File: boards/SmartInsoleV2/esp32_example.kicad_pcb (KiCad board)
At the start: 2 copper layers, 57.2 x 79.5 mm, 104 parts, among them J1 Screw_Terminal_01x02, J2 USB_B_Micro, J3 Conn_01x05_Female, J4 Screw_Terminal_01x02, J5 Conn_01x09_Female, J6 Conn_01x08_Female, J7 Conn_ARM_JTAG_SWD_10, J8 Screw_Terminal_01x02, Q1 AO4485, Q2 SS8050-G, Q3 SS8050-G, SW1 SW_Push, SW2 SW_Push, U1 INA240A1D, U2 MAX14871EUE+, U3 OPA2340, U4 INA240A1D, U5 MAX14871EUE+, U6 TPS62933ODRLR, U7 ESP32-S3-WROOM-1-N16R2

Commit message: a little progress
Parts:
- removed C10, C11, C12: 10u, Resistor_SMD:R_1206_3216Metric
- removed C13, C14, C15, C21, C25, C5, C6, C9: 100n, Capacitor_SMD:C_0805_2012Metric
- removed C16, C20: 10u, Capacitor_SMD:C_0805_2012Metric
- removed C17, C22, C7, C8: DNP, Capacitor_SMD:C_0805_2012Metric
- removed C26, C27: 33u, Capacitor_SMD:C_0805_2012Metric
- removed D2: D_Zener, local_footprints:SOD-123_ONS
- removed D4: D_Schottky, Diode_SMD:D_SMA
- removed F1: Fuse, Fuse:Fuseholder_Littelfuse_Nano2_154x
- removed J5: Conn_01x09_Female, Connector_PinHeader_2.54mm:PinHeader_1x09_P2.54mm_Vertical
- removed J6: Conn_01x08_Female, Connector_PinHeader_2.54mm:PinHeader_1x08_P2.54mm_Vertical
- removed J8: Screw_Terminal_01x02, TerminalBlock_Phoenix:TerminalBlock_Phoenix_MKDS-1,5-2-5.08_1x02_P5.08mm_Horizontal
- removed JP3: SolderJumper_2_Open, Jumper:SolderJumper-2_P1.3mm_Open_TrianglePad1.0x1.5mm
- removed L1: 4.7u, Inductor_SMD:L_Taiyo-Yuden_NR-60xx
- removed Q1: AO4485, local_footprints:SO8SOP-8L_AOS
- removed R23, R26: DNP, Resistor_SMD:R_0805_2012Metric
- removed R27, R28, R29: 100k, Resistor_SMD:R_0805_2012Metric
- removed R30: 31.3k, Resistor_SMD:R_0805_2012Metric
- removed R31: 10.0k, Resistor_SMD:R_0805_2012Metric
- removed R9: 10k, Resistor_SMD:R_0805_2012Metric
- removed TP1, TP10, TP12, TP13, TP2, TP3, TP4, TP5, TP6, TP7, TP8, TP9: TestPoint, TestPoint:TestPoint_Keystone_5010-5014_Multipurpose
- removed TP11: TestPoint, TestPoint:TestPoint_Pad_D2.0mm
- removed U2, U5: MAX14871EUE+, local_footprints:21-0108_U16E&plus_3_MXM
- removed U4: INA240A1D, Package_SO:SOIC-8_3.9x4.9mm_P1.27mm
- removed U6: TPS62933ODRLR, local_footprints:SOT5X3-8_DRL_TEX
- added SW3: SW_Push, Button_Switch_SMD:SW_SPST_B3S-1000, F.Cu at (97.4, 85.1)
- added SW4: SW_Push, Button_Switch_SMD:SW_SPST_B3S-1000, F.Cu at (97.4, 93.6)
- C1, C2: value 10u -> 1uF; footprint Resistor_SMD:R_1206_3216Metric -> Capacitor_SMD:C_0603_1608Metric
- C3: value 10u -> 10uF; footprint Resistor_SMD:R_1206_3216Metric -> Capacitor_SMD:C_0603_1608Metric
- C4: value 100n -> 10uF; footprint Capacitor_SMD:C_0805_2012Metric -> Capacitor_SMD:C_0603_1608Metric
- D3: value BAT54S -> LED; footprint Package_TO_SOT_SMD:SOT-23 -> LED_SMD:LED_0603_1608Metric
- J1: value Screw_Terminal_01x02 -> Conn_01x02_Pin; footprint TerminalBlock_Phoenix:TerminalBlock_Phoenix_MKDS-1,5-2-5.08_1x02_P5.08mm_Horizontal -> Connector_JST:JST_PH_B2B-PH-K_1x02_P2.00mm_Vertical
- J4: value Screw_Terminal_01x02 -> Conn_02x10_Odd_Even; footprint TerminalBlock_Phoenix:TerminalBlock_Phoenix_MKDS-1,5-2-5.08_1x02_P5.08mm_Horizontal -> Connector_PinHeader_2.54mm:PinHeader_2x10_P2.54mm_Vertical
- JP1, R12: moved to F.Cu
- R1, R15: value 20m -> 1k; footprint Resistor_SMD:R_1206_3216Metric -> Resistor_SMD:R_0603_1608Metric
- R10, R11: value 100k -> 1k; footprint Resistor_SMD:R_0805_2012Metric -> Resistor_SMD:R_0603_1608Metric
- R16, R2: value DNP -> 1k; footprint Resistor_SMD:R_0805_2012Metric -> Resistor_SMD:R_0603_1608Metric
- R20: value 1k -> 1M; footprint Resistor_SMD:R_0805_2012Metric -> Resistor_SMD:R_0603_1608Metric
- R21: value 0 -> 200k; footprint Resistor_SMD:R_0805_2012Metric -> Resistor_SMD:R_0603_1608Metric
- R22: value DNP -> 5.1k; footprint Resistor_SMD:R_0805_2012Metric -> Resistor_SMD:R_0603_1608Metric
- R3, R4: value 4.7k -> 1k; footprint Resistor_SMD:R_0805_2012Metric -> Resistor_SMD:R_0603_1608Metric
- R5: footprint Resistor_SMD:R_0805_2012Metric -> Resistor_SMD:R_0603_1608Metric
- R6, R8: value 100k -> 5k; footprint Resistor_SMD:R_0805_2012Metric -> Resistor_SMD:R_0603_1608Metric
- R7: value 0 -> 1k; footprint Resistor_SMD:R_0805_2012Metric -> Resistor_SMD:R_0603_1608Metric
- U1: value INA240A1D -> MPU-6050; footprint Package_SO:SOIC-8_3.9x4.9mm_P1.27mm -> Sensor_Motion:InvenSense_QFN-24_4x4mm_P0.5mm
- U3: value OPA2340 -> TLV75801PDRV; footprint Package_SO:SOIC-8_3.9x4.9mm_P1.27mm -> Package_SON:WSON-6-1EP_2x2mm_P0.65mm_EP1x1.6mm
- moved H2 120.1 mm to (218.9, 52.4)
- moved H4 108.5 mm to (221.2, 119.6)
- moved J2 103.3 mm to (207.3, 69.5), turned to 90 degrees
- moved R11 83.7 mm to (185.2, 87.7), turned to -90 degrees
- moved J4 75.9 mm to (167.8, 96.4), turned to 90 degrees
- moved R1 74.6 mm to (167.7, 87.7), turned to -90 degrees
- moved R15 74.2 mm to (187.6, 87.7), turned to -90 degrees
- moved JP1 72.4 mm to (99.0, 104.2), turned to 0 degrees
- moved R20 68.3 mm to (132.9, 97.9), turned to 0 degrees
- moved R2 68.3 mm to (170.2, 87.7), turned to -90 degrees
- moved R16 67.6 mm to (190.0, 87.7), turned to -90 degrees
- moved SW2 67.3 mm to (97.4, 76.7), turned to 0 degrees
- moved Q3 63.6 mm to (94.3, 104.8), turned to 0 degrees
- moved Q2 63.6 mm to (94.3, 100.2), turned to 0 degrees
- moved R21 61.8 mm to (132.9, 100.4), turned to 0 degrees
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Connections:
- C1 pad 1: +BATT -> /End Hike
- C2 pad 1: +BATT -> /Start Hike
- C3 pad 1: +BATT -> /POWER FROM BATTERY
- C4 pad 1: +BATT -> +3V3
- D3 pad 2: +3V3 -> Net-(D3-A)
- J1 pad 1: GND -> /POWER FROM BATTERY
- J1 pad 2: Net-(F1-Pad1) -> GND
- J4 pad 1: /M1- -> /PRESS1
- J4 pad 2: Net-(J4-Pad2) -> GND
- R1 pad 1: Net-(J4-Pad2) -> /PRESS1
- R1 pad 2: /M1+ -> +3V3
- R10 pad 1: /M1_FAULT -> /PRESS7
- R11 pad 1: Net-(R11-Pad1) -> /PRESS8
- R15 pad 1: Net-(J8-Pad2) -> /PRESS9
- R15 pad 2: /M2+ -> +3V3
- R16 pad 1: GND -> /PRESS10
- R16 pad 2: Net-(R16-Pad2) -> +3V3
- R2 pad 1: GND -> /PRESS2
- R2 pad 2: Net-(R2-Pad2) -> +3V3
- R20 pad 1: Net-(R20-Pad1) -> Net-(U3-FB)
- R20 pad 2: Net-(C15-Pad1) -> +3V3
- R21 pad 1: Net-(C15-Pad1) -> GND
- R21 pad 2: Net-(C17-Pad1) -> Net-(U3-FB)
- R22 pad 1: +BATT -> +3V3
- R22 pad 2: Net-(R22-Pad2) -> Net-(D3-A)
- R3 pad 1: +3V3 -> /PRESS3
- R3 pad 2: /CAMERA_SDA -> +3V3
- R4 pad 1: +3V3 -> /PRESS4
- R4 pad 2: /CAMERA_SCL -> +3V3
- R5 pad 1: Net-(R5-Pad1) -> /PRESS5
- R5 pad 2: Net-(C6-Pad1) -> +3V3
- R6 pad 2: GND -> /End Hike
- R7 pad 1: Net-(C6-Pad1) -> /PRESS6
- R7 pad 2: Net-(C7-Pad1) -> +3V3
- R8 pad 1: +BATT -> Net-(R8-Pad1)
- R8 pad 2: /VBAT_SENSE -> /Start Hike
- U1 pad 1: Net-(J4-Pad2) -> unconnected-(U1-CLKIN-Pad1)
- U1 pad 2: GND -> unconnected-(U1-NC-Pad2)
- U1 pad 3: GND -> unconnected-(U1-NC-Pad3)
- U1 pad 4: GND -> unconnected-(U1-NC-Pad4)
- U1 pad 5: Net-(R5-Pad1) -> unconnected-(U1-NC-Pad5)
- U1 pad 6: +3V3 -> unconnected-(U1-AUX_DA-Pad6)
- U1 pad 7: +3V3 -> unconnected-(U1-AUX_CL-Pad7)
- U1 pad 8: /M1+ -> +3V3
- U3 pad 1: /I_M_1 -> +3V3
- U3 pad 2: /I_M_1 -> Net-(U3-FB)
- U3 pad 3: Net-(C7-Pad1) -> GND
- U3 pad 4: GND -> /POWER FROM BATTERY
- U3 pad 5: Net-(C17-Pad1) -> unconnected-(U3-DNC-Pad5)
- U3 pad 6: /I_M_2 -> /POWER FROM BATTERY
- U3 pad 7: /I_M_2 -> GND
- U7 pad 10: /GPIO17 -> /End Hike
- U7 pad 11: /GPIO18 -> /PRESS1
- U7 pad 12: /M1_FAULT -> /PRESS2
- U7 pad 17: /M1_EN -> /PRESS3
- U7 pad 18: /M1_PWM -> /PRESS4
- U7 pad 19: /M1_DIR -> /PRESS5
- U7 pad 20: /M2_FAULT -> /PRESS6
- U7 pad 21: /M2_EN -> /PRESS7
- U7 pad 22: /M2_PWM -> /PRESS8
- U7 pad 23: /M2_DIR -> /PRESS9
- U7 pad 24: /CAMERA_CS -> /PRESS10
- U7 pad 25: /CAMERA_MOSI -> unconnected-(U7-IO48-Pad25)
- U7 pad 28: /CAMERA_MISO -> /CS
- U7 pad 29: /CAMERA_SCK -> /MISO
- U7 pad 30: /CAMERA_SDA -> /MOSI
- U7 pad 31: /CAMERA_SCL -> /SCLK
- U7 pad 38: /I_M_1 -> /SCL_6050
- U7 pad 39: /I_M_2 -> /SDA_6050
- U7 pad 5: /GPIO5 -> unconnected-(U7-IO5-Pad5)
- U7 pad 6: /GPIO6 -> unconnected-(U7-IO6-Pad6)
- U7 pad 7: /GPIO7 -> unconnected-(U7-IO7-Pad7)
- U7 pad 8: /GPIO15 -> unconnected-(U7-IO15-Pad8)
- U7 pad 9: /GPIO16 -> /Start Hike
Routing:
- net +3V3: track 283.9 -> 0.00 mm, vias 21 -> 0
- net /M1_FAULT: track 70.8 -> 0.00 mm, vias 2 -> 0
- net /I_M_2: track 67.9 -> 0.00 mm, vias 2 -> 0
- net /M1_EN: track 64.0 -> 0.00 mm
- net /I_M_1: track 62.9 -> 0.00 mm, vias 2 -> 0
- net /M1_PWM: track 60.5 -> 0.00 mm
- net /M1_DIR: track 57.4 -> 0.00 mm
- net Net-(R5-Pad1): track 53.0 -> 0.00 mm
- net /M2_DIR: track 52.4 -> 0.00 mm
- net /M2_PWM: track 51.4 -> 0.00 mm
- net +BATT: track 50.1 -> 0.00 mm, vias 34 -> 0
- net /M2_EN: track 48.9 -> 0.00 mm
- net /M2_FAULT: track 48.3 -> 0.00 mm
- net /CAMERA_CS: track 48.2 -> 0.00 mm
- net /CAMERA_MOSI: track 44.8 -> 0.00 mm
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- removed copper zone on B.Cu, net +3V3
- removed copper zone on F.Cu, net +3V3
- removed copper zone on B.Cu, net +BATT
- removed copper zone on F.Cu, net +BATT
- removed copper zone on F.Cu, net /M1+
- removed copper zone on F.Cu, net /M1-
- removed copper zone on F.Cu, net /M2+
- removed copper zone on F.Cu, net /M2-
- removed copper zone on B.Cu, net GND
- removed copper zone on F.Cu, net GND
- removed copper zone on F.Cu, net Net-(C25-Pad2)
- removed copper zone on F.Cu, net Net-(C26-Pad1)
- removed copper zone on F.Cu, net Net-(F1-Pad1)
- removed copper zone on F.Cu, net Net-(F1-Pad2)
- removed copper zone on F.Cu, net Net-(J4-Pad2)
- removed copper zone on F.Cu, net Net-(J8-Pad2)
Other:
- board outline removed
- board text removed: "+"
- board text removed: "-"
- board text removed: "ESP32 Motor Controller Rev A Jason Paximadas"

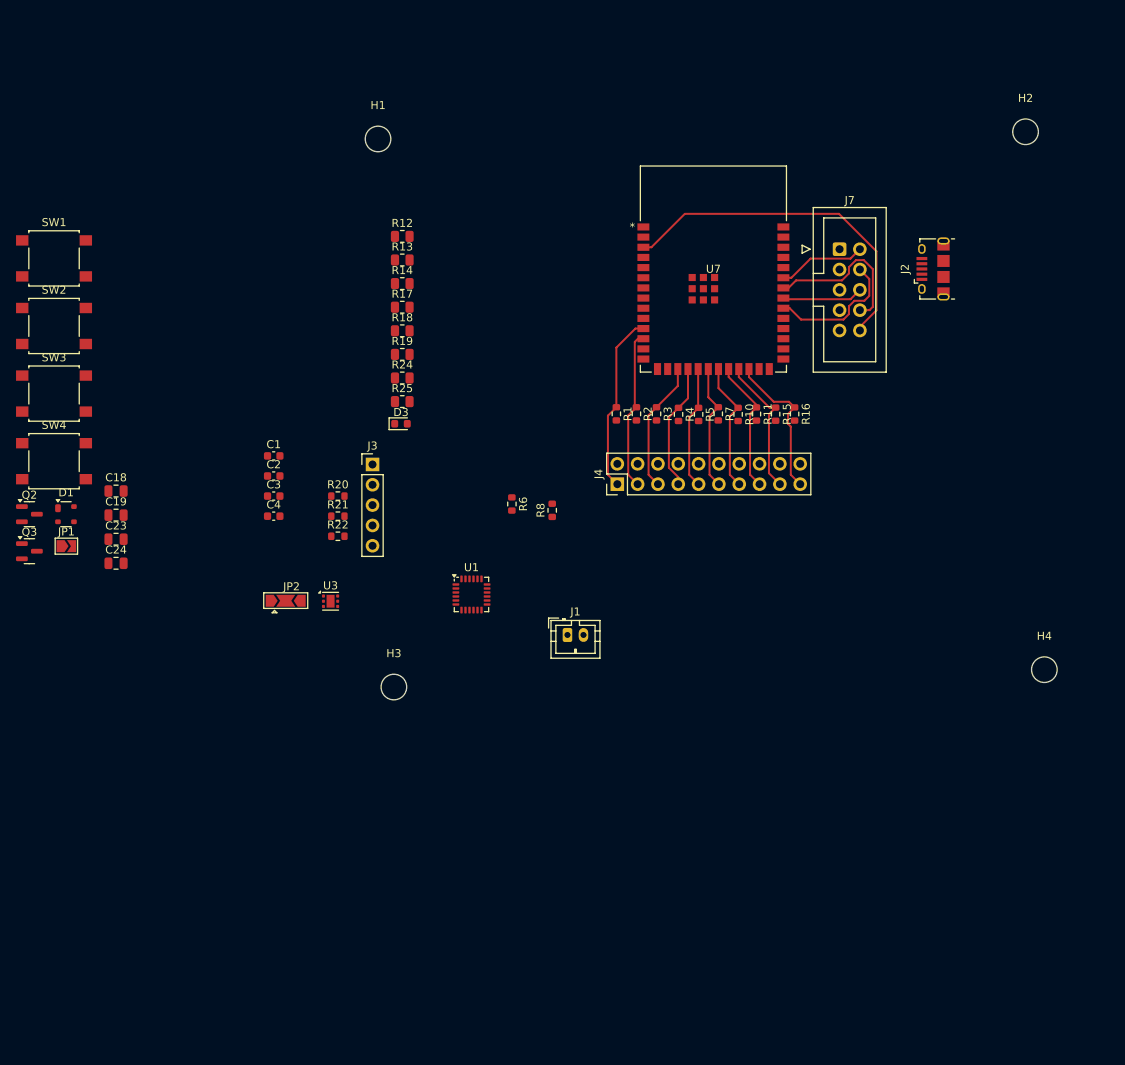
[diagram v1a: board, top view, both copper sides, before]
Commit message: Most of routing done
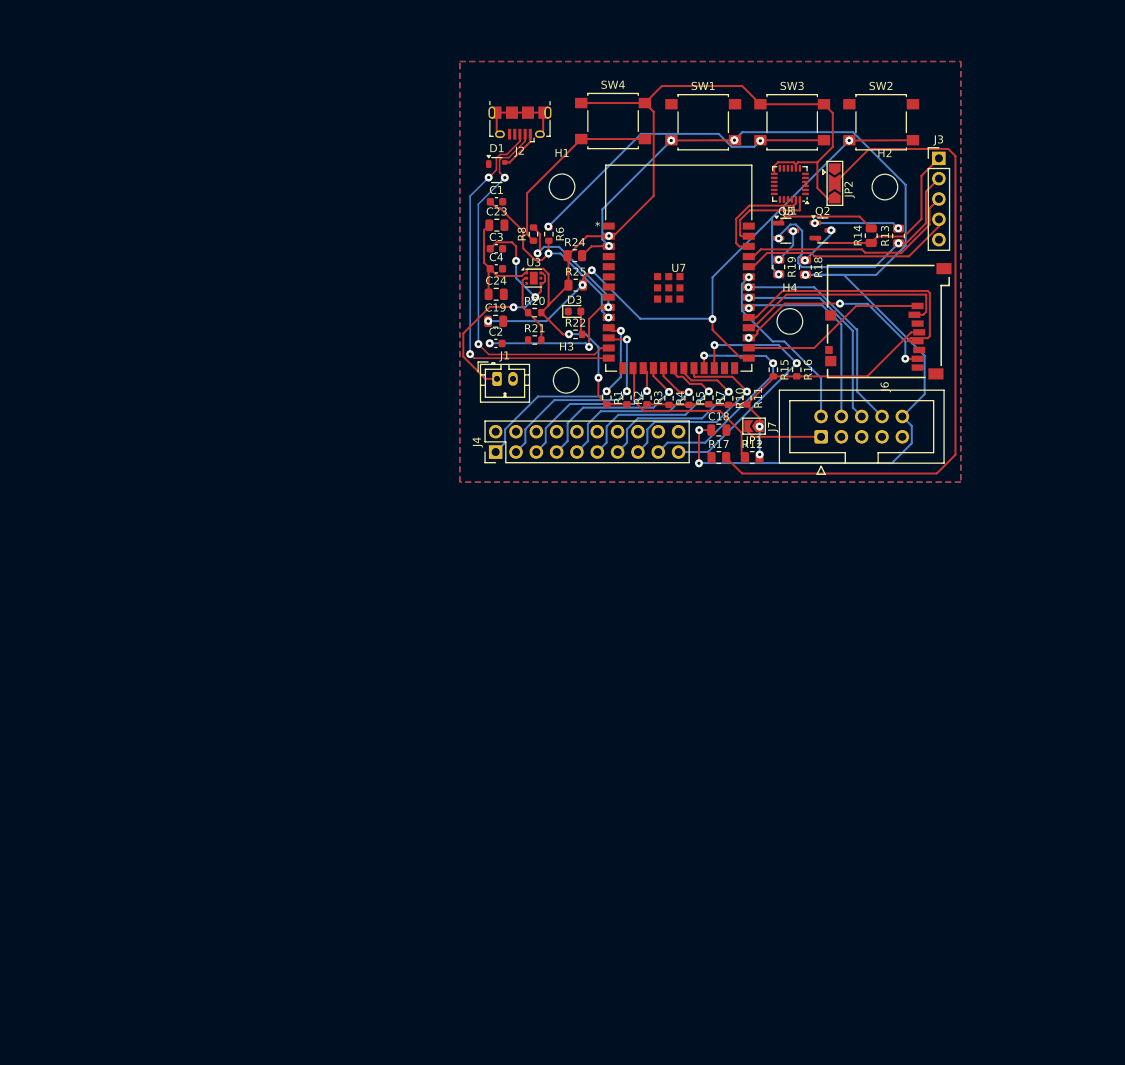
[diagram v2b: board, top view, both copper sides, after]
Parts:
- added J6: PJS008U-3000-0, MEM2051-00-195-00-A:GCT_MEM2051-00-195-00-A, F.Cu at (201.7, 76.1)
- moved SW2 106.5 mm to (200.8, 51.2)
- moved Q2 105.3 mm to (193.5, 64.7)
- moved Q3 102.7 mm to (188.9, 64.8)
- moved SW3 98.3 mm to (189.7, 51.2)
- moved JP1 87.3 mm to (184.9, 89.2), turned to 180 degrees
- moved JP2 86.2 mm to (195.0, 58.8), turned to -90 degrees
- moved SW1 82.9 mm to (178.6, 51.2)
- moved SW4 81.8 mm to (167.3, 51.0)
- moved J3 80.5 mm to (208.0, 55.7)
- moved C18 75.7 mm to (180.5, 89.7)
- moved D1 68.9 mm to (152.8, 57.2)
- moved U1 64.9 mm to (189.4, 58.9), turned to 180 degrees
- moved R13 62.1 mm to (203.0, 65.4), turned to 90 degrees
- moved C23 61.7 mm to (152.8, 64.1)
- moved R14 58.9 mm to (199.6, 65.4), turned to 90 degrees
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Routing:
- net +3V3: track 0.00 -> 174.3 mm, vias 0 -> 5
- net /CHIP_PU: track 43.6 -> 140.3 mm, vias 0 -> 6
- net /GPIO0_STRAPPING: track 0.00 -> 86.1 mm, vias 0 -> 6
- net Net-(JP2-C): track 0.00 -> 85.0 mm
- net /D+: track 0.00 -> 48.1 mm, vias 0 -> 2
- net /D-: track 0.00 -> 47.3 mm, vias 0 -> 2
- net Net-(R6-Pad1): track 0.00 -> 40.2 mm, vias 0 -> 2
- net /Start Hike: track 0.00 -> 36.8 mm, vias 0 -> 4
- net /POWER FROM BATTERY: track 0.00 -> 34.5 mm, vias 0 -> 3
- net /SCLK: track 0.00 -> 33.8 mm
- net /DTR: track 0.00 -> 33.1 mm, vias 0 -> 2
- net /TX: track 0.00 -> 28.3 mm
- net /MOSI: track 0.00 -> 27.7 mm
- net /MISO: track 0.00 -> 27.3 mm, vias 0 -> 3
- net /RX: track 0.00 -> 27.1 mm
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- added copper zone on B.Cu, net GND
- added copper zone on F.Cu, net GND

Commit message: added changes but not finished
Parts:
- removed H1, H2, H3, H4: MountingHole, MountingHole:MountingHole_3.2mm_M3
- removed SW3, SW4: SW_Push, Button_Switch_SMD:SW_SPST_B3S-1000
- added J5: Conn_01x02_Pin, Connector_PinHeader_2.54mm:PinHeader_1x02_P2.54mm_Vertical, F.Cu at (162.8, 60.0)
- added J8: Conn_01x02_Pin, Connector_PinHeader_2.54mm:PinHeader_1x02_P2.54mm_Vertical, F.Cu at (162.4, 56.0)
- moved C23 10.9 mm to (163.2, 67.2)
- moved J2 7.88 mm to (155.5, 59.2)
- moved C1 7.50 mm to (157.5, 66.9)
- moved D1 6.56 mm to (152.7, 63.7)
- moved R24 5.45 mm to (161.8, 73.3)
- moved R6 5.35 mm to (159.3, 70.5)
- moved R8 5.35 mm to (157.4, 70.5)
- moved U3 5.24 mm to (156.1, 75.8)
- moved R25 4.80 mm to (163.2, 76.3)
- moved D3 3.94 mm to (163.2, 78.7)
- moved R20 3.82 mm to (158.8, 78.6)
- moved C19 3.15 mm to (154.5, 78.6)
- moved R22 2.91 mm to (163.2, 80.6)
- moved C2 2.52 mm to (154.6, 80.5)
- moved R21 2.51 mm to (158.9, 80.5)
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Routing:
- net +3V3: track 174.3 -> 58.6 mm, vias 5 -> 10
- net Net-(J8-Pin_1): track 23.8 -> 1.13 mm
- net /POWER FROM BATTERY: track 34.5 -> 24.6 mm, vias 3 -> 2
- net /D+: track 48.1 -> 40.8 mm
- net /End Hike: track 26.0 -> 19.9 mm
- net /D-: track 47.3 -> 41.2 mm
- net Net-(J5-Pin_1): track 40.2 -> 45.6 mm
- net /CHIP_PU: track 140.3 -> 145.3 mm
- net /Start Hike: track 36.8 -> 32.9 mm
- net Net-(D3-A): track 2.94 -> 1.86 mm
- net Net-(U3-FB): track 9.04 -> 8.03 mm
- net Net-(JP2-C): track 85.0 -> 84.4 mm
- net +5V: track 5.20 -> 4.61 mm
- added copper zone on B.Cu, net +3V3
- removed copper zone on B.Cu, net GND

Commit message: re made board
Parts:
- removed J6: PJS008U-3000-0, MEM2051-00-195-00-A:GCT_MEM2051-00-195-00-A
- C1, C2, C3, C4: footprint Capacitor_SMD:C_0603_1608Metric -> Capacitor_SMD:C_0805_2012Metric
- D3: footprint LED_SMD:LED_0603_1608Metric -> LED_SMD:LED_0805_2012Metric
- JP1, JP2: moved to B.Cu
- R1, R10, R11, R15, R16, R2, R3, R4, R5, R6, R7, R8: footprint Resistor_SMD:R_0603_1608Metric -> Resistor_SMD:R_0805_2012Metric
- moved C24 58.9 mm to (205.8, 44.3)
- moved J2 57.5 mm to (211.2, 45.0), turned to 90 degrees
- moved D1 55.8 mm to (206.2, 48.1)
- moved J4 53.4 mm to (202.9, 74.4), turned to -90 degrees
- moved J5 52.4 mm to (212.4, 76.7), turned to 180 degrees
- moved J8 50.7 mm to (208.7, 76.7), turned to 180 degrees
- moved C23 49.8 mm to (205.8, 41.5)
- moved R8 48.9 mm to (205.8, 77.1)
- moved R6 46.6 mm to (205.8, 73.6)
- moved J3 41.5 mm to (166.7, 59.2)
- moved R13 40.3 mm to (169.3, 43.3), turned to 0 degrees
- moved R1 39.6 mm to (202.9, 70.2), turned to 90 degrees
- moved R14 38.7 mm to (169.3, 41.2), turned to 0 degrees
- moved C18 36.3 mm to (173.3, 54.2)
- moved R12 35.7 mm to (173.2, 59.3), turned to 180 degrees
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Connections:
- U7 pad 11: /PRESS1 -> /PRESS8
- U7 pad 12: /PRESS2 -> /SDA_6050
- U7 pad 17: /PRESS3 -> /SCL_6050
- U7 pad 18: /PRESS4 -> /PRESS5
- U7 pad 19: /PRESS5 -> /PRESS4
- U7 pad 20: /PRESS6 -> /PRESS3
- U7 pad 21: /PRESS7 -> /PRESS2
- U7 pad 22: /PRESS8 -> /PRESS1
- U7 pad 23: /PRESS9 -> unconnected-(U7-IO21-Pad23)
- U7 pad 24: /PRESS10 -> unconnected-(U7-IO47-Pad24)
- U7 pad 38: /SCL_6050 -> unconnected-(U7-IO2-Pad38)
- U7 pad 39: /SDA_6050 -> unconnected-(U7-IO1-Pad39)
- U7 pad 5: unconnected-(U7-IO5-Pad5) -> /PRESS6
- U7 pad 6: unconnected-(U7-IO6-Pad6) -> /PRESS7
- U7 pad 7: unconnected-(U7-IO7-Pad7) -> /PRESS10
- U7 pad 8: unconnected-(U7-IO15-Pad8) -> /PRESS9
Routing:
- net /CHIP_PU: track 145.3 -> 62.9 mm, vias 6 -> 2
- net Net-(JP2-C): track 84.4 -> 4.79 mm, vias 0 -> 1
- net /Start Hike: track 32.9 -> 103.1 mm, vias 4 -> 3
- net /End Hike: track 19.9 -> 82.6 mm, vias 2 -> 3
- net /GPIO0_STRAPPING: track 86.3 -> 48.9 mm, vias 6 -> 4
- net Net-(J5-Pin_1): track 45.6 -> 8.56 mm, vias 2 -> 0
- net /TX: track 28.3 -> 62.4 mm, vias 0 -> 2
- net /SCLK: track 33.8 -> 0.00 mm
- net /RX: track 27.1 -> 60.4 mm, vias 0 -> 2
- net /PRESS6: track 24.9 -> 55.7 mm, vias 1 -> 2
- net /MOSI: track 27.7 -> 0.00 mm
- net /MISO: track 27.3 -> 0.00 mm, vias 3 -> 0
- net /PRESS7: track 25.2 -> 51.7 mm, vias 1 -> 2
- net +3V3: track 58.6 -> 33.3 mm, vias 10 -> 23
- net /CS: track 23.3 -> 0.00 mm
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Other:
- board outline added: 49 x 38.4 mm
